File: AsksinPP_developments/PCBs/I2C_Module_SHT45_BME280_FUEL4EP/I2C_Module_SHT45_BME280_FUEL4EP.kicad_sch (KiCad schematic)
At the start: 14 parts, among them J1 Conn_01x04, J2 Conn_01x04, U1 BME280, U2 SHT45-AD1F-R2

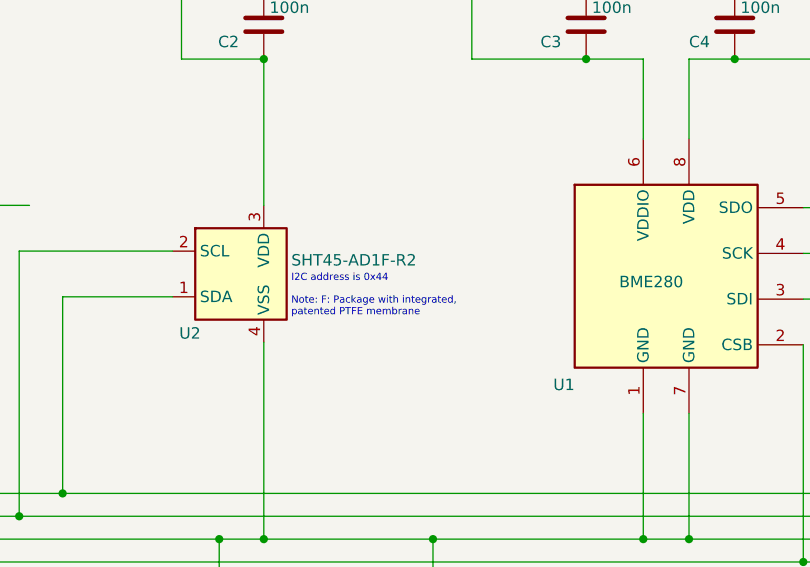
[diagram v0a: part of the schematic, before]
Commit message: PCBs: HB_TH_Sensor_SHT45_AllInOne_FUEL4EP and I2C_Module_SHT45_BME280_FUEL4EP: replacement of SHT45 to type without PTFE filter
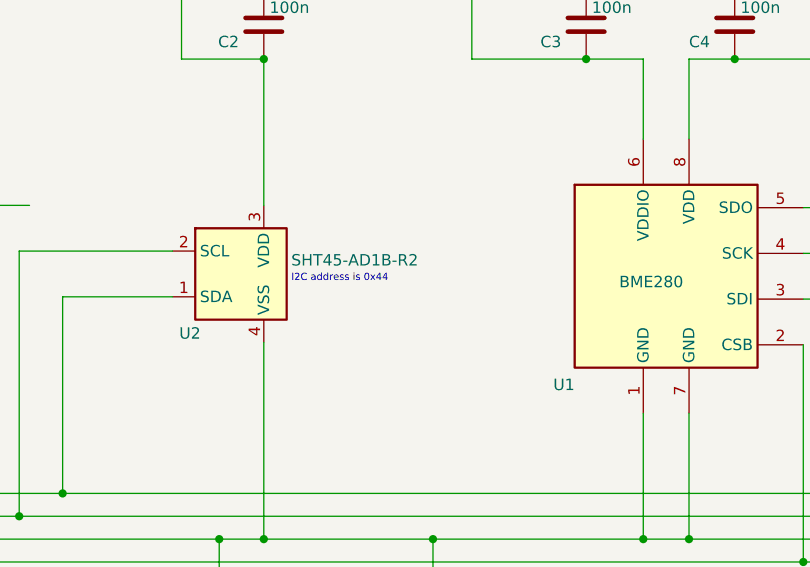
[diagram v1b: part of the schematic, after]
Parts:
- U2: value SHT45-AD1F-R2 -> SHT45-AD1B-R2; LCSC C5360602 -> C5221601
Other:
- note removed: "Note: F: Package with integrated, patented PTFE membrane"
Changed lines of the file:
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@@
   (title_block
     (title "I2C_Module_SHT45_BME280_FUEL4EP")
-    (date "2023-09-09")
-    (rev "1.0")
+    (date "2023-12-15")
+    (rev "1.1")
     (company "FUEL4EP")
     (comment 1 "fitting to  HB-UNI-SEN-BATT_ATMega1284P_E07-868MS10_FUEL4EP")
@@
     (stroke (width 0) (type default) (color 0 0 0 0))
   )
-  (text "Note: F: Package with integrated,\npatented PTFE membrane"
-    (at 105.664 87.122 0)
-    (effects (font (size 0.8 0.8)) (justify left bottom))
-  )
   (text "cut JP1 for I2C address 0x77\n" (at 163.83 74.295 0)
     (effects (font (size 0.8 0.8)) (justify left bottom))
@@
       (effects (font (size 1.27 1.27)) (justify left))
     )
-    (property "Value" "SHT45-AD1F-R2" (id 1) (at 105.664 80.772 0)
+    (property "Value" "SHT45-AD1B-R2" (id 1) (at 105.664 80.772 0)
       (effects (font (size 1.27 1.27)) (justify left))
     )
@@
       (effects (font (size 1.27 1.27)) (justify left) hide)
     )
-    (property "Datasheet" "https://sensirion.com/media/documents/33FD6951/624C4357/Datasheet_SHT4x.pdf" (id 3) (at 103.886 91.186 0)
+    (property "Datasheet" "https://sensirion.com/media/documents/33FD6951/6555C40E/Sensirion_Datasheet_SHT4x.pdf" (id 3) (at 103.886 91.186 0)
       (effects (font (size 1.27 1.27)) (justify left) hide)
     )
-    (property "LCSC" "C5360602" (id 4) (at 100.076 82.296 0)
+    (property "LCSC" "C5221601" (id 4) (at 100.076 82.296 0)
       (effects (font (size 1.524 1.524)) hide)
     )
@@
     )
     (path "/4286b13a-2c83-4a2b-871b-df5ad20905f3"
-      (reference "U2") (unit 1) (value "SHT45-AD1F-R2") (footprint "FUEL4EP:SHT4X")
-    )
-  )
+      (reference "U2") (unit 1) (value "SHT45-AD1B-R2") (footprint "FUEL4EP:SHT4X")
+    )
+  )

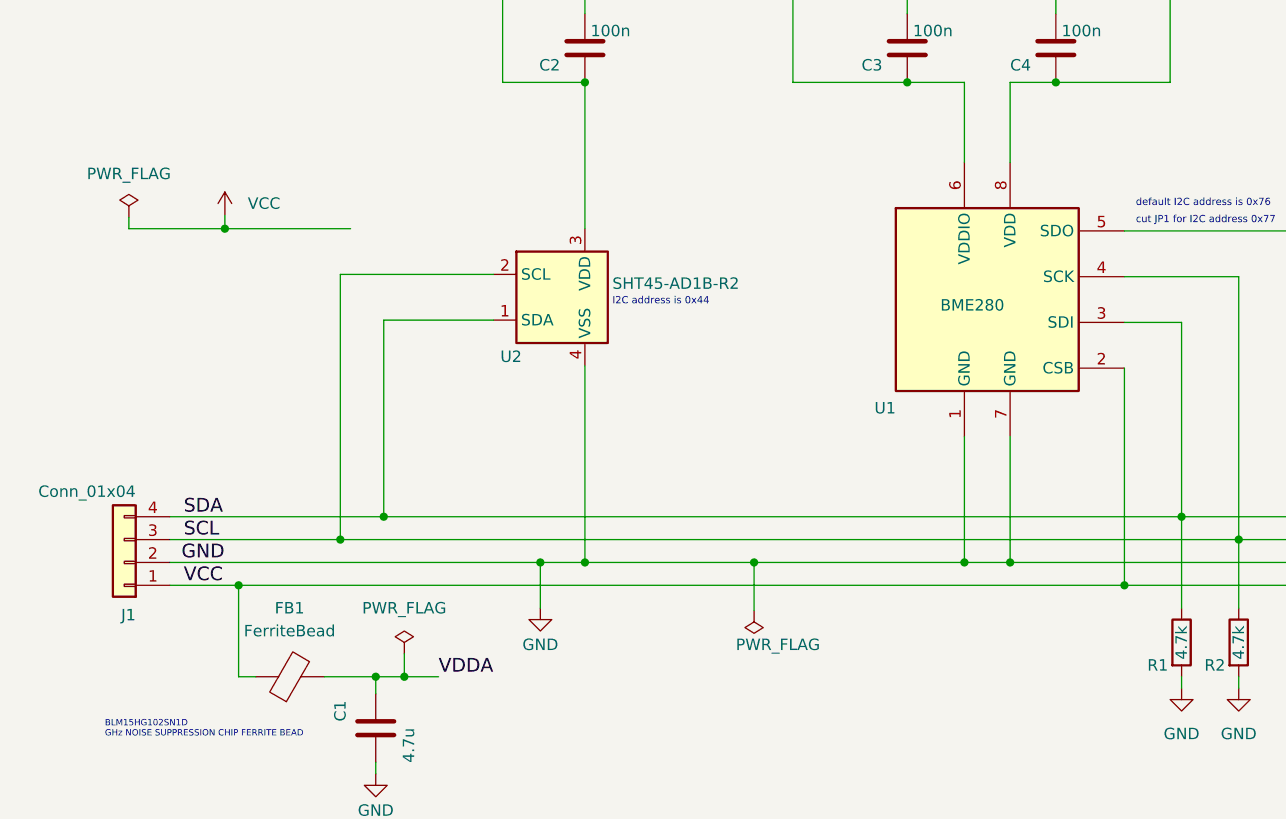
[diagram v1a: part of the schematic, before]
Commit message: PCBs: fix of some project specific KiCAD library paths for portability and missing PWR_FLGs for VCC in some schematics
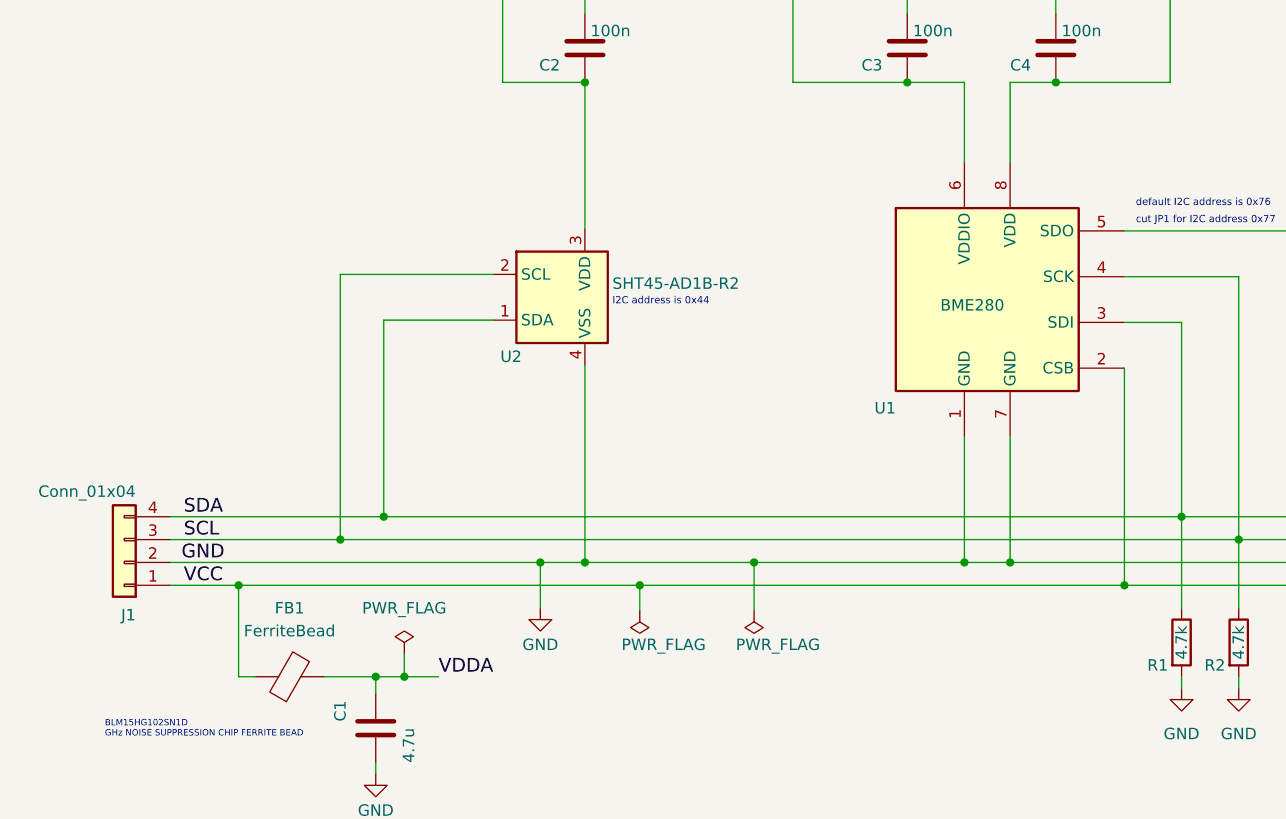
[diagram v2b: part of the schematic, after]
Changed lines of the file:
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@@
   (title_block
     (title "I2C_Module_SHT45_BME280_FUEL4EP")
-    (date "2023-12-15")
-    (rev "1.1")
+    (date "2024-01-14")
+    (rev "1.2")
     (company "FUEL4EP")
     (comment 1 "fitting to  HB-UNI-SEN-BATT_ATMega1284P_E07-868MS10_FUEL4EP")
@@
   (junction (at 149.86 111.76) (diameter 0) (color 0 0 0 0)
   )
-  (junction (at 62.611 74.676) (diameter 0) (color 0 0 0 0)
-  )
   (junction (at 154.94 58.42) (diameter 0) (color 0 0 0 0)
   )
@@
   (junction (at 82.55 124.46) (diameter 0) (color 0 0 0 0)
   )
+  (junction (at 108.712 114.3) (diameter 0) (color 0 0 0 0)
+  )
   (junction (at 102.616 111.76) (diameter 0) (color 0 0 0 0)
   )
@@
     (stroke (width 0) (type default) (color 0 0 0 0))
   )
-  (wire (pts (xy 51.943 74.676) (xy 51.943 73.406))
-    (stroke (width 0) (type default) (color 0 0 0 0))
-  )
   (wire (pts (xy 138.43 48.26) (xy 138.43 50.8))
     (stroke (width 0) (type default) (color 0 0 0 0))
@@
     (stroke (width 0) (type default) (color 0 0 0 0))
   )
-  (wire (pts (xy 62.611 74.676) (xy 51.943 74.676))
+  (wire (pts (xy 108.712 114.3) (xy 162.56 114.3))
     (stroke (width 0) (type default) (color 0 0 0 0))
   )
@@
     (stroke (width 0) (type default) (color 0 0 0 0))
   )
-  (wire (pts (xy 62.611 74.676) (xy 62.611 73.152))
-    (stroke (width 0) (type default) (color 0 0 0 0))
-  )
   (wire (pts (xy 125.73 58.42) (xy 138.43 58.42))
     (stroke (width 0) (type default) (color 0 0 0 0))
   )
-  (wire (pts (xy 64.135 114.3) (xy 162.56 114.3))
+  (wire (pts (xy 64.135 114.3) (xy 108.712 114.3))
     (stroke (width 0) (type default) (color 0 0 0 0))
   )
@@
     (stroke (width 0) (type default) (color 0 0 0 0))
   )
-  (wire (pts (xy 62.611 74.676) (xy 76.581 74.676))
-    (stroke (width 0) (type default) (color 0 0 0 0))
-  )
   (wire (pts (xy 56.515 111.76) (xy 97.663 111.76))
+    (stroke (width 0) (type default) (color 0 0 0 0))
+  )
+  (wire (pts (xy 108.712 114.3) (xy 108.712 117.094))
     (stroke (width 0) (type default) (color 0 0 0 0))
   )
@@
     (pin "8")
   )
-  (symbol (lib_id "power:VCC") (at 62.611 73.152 0) (unit 1)
-    (in_bom yes) (on_board yes) (fields_autoplaced)
-    (property "Reference" "#PWR01" (id 0) (at 62.611 76.962 0)
-      (effects (font (size 1.27 1.27)) hide)
-    )
-    (property "Value" "VCC" (id 1) (at 65.151 71.8819 0)
-      (effects (font (size 1.27 1.27)) (justify left))
-    )
-    (property "Footprint" "" (id 2) (at 62.611 73.152 0)
-      (effects (font (size 1.27 1.27)) hide)
-    )
-    (property "Datasheet" "" (id 3) (at 62.611 73.152 0)
-      (effects (font (size 1.27 1.27)) hide)
-    )
-    (pin "1")
-  )
   (symbol (lib_id "Device:C") (at 79.375 130.175 0) (unit 1)
     (in_bom yes) (on_board yes)
@@
     (pin "1")
   )
-  (symbol (lib_id "power:PWR_FLAG") (at 51.943 73.406 0) (unit 1)
-    (in_bom yes) (on_board yes) (fields_autoplaced)
-    (property "Reference" "#FLG01" (id 0) (at 51.943 71.501 0)
-      (effects (font (size 1.27 1.27)) hide)
-    )
-    (property "Value" "PWR_FLAG" (id 1) (at 51.943 68.58 0))
-    (property "Footprint" "" (id 2) (at 51.943 73.406 0)
-      (effects (font (size 1.27 1.27)) hide)
-    )
-    (property "Datasheet" "~" (id 3) (at 51.943 73.406 0)
-      (effects (font (size 1.27 1.27)) hide)
-    )
-    (pin "1")
-  )
   (symbol (lib_id "power:PWR_FLAG") (at 121.412 117.094 180) (unit 1)
     (in_bom yes) (on_board yes)
@@
     (pin "2")
   )
+  (symbol (lib_id "power:PWR_FLAG") (at 108.712 117.094 180) (unit 1)
+    (in_bom yes) (on_board yes)
+    (property "Reference" "#FLG0102" (id 0) (at 108.712 118.999 0)
+      (effects (font (size 1.27 1.27)) hide)
+    )
+    (property "Value" "PWR_FLAG" (id 1) (at 106.68 120.904 0)
+      (effects (font (size 1.27 1.27)) (justify right))
+    )
+    (property "Footprint" "" (id 2) (at 108.712 117.094 0)
+      (effects (font (size 1.27 1.27)) hide)
+    )
+    (property "Datasheet" "~" (id 3) (at 108.712 117.094 0)
+      (effects (font (size 1.27 1.27)) hide)
+    )
+    (pin "1")
+  )
   (sheet_instances
     (path "/" (page "1"))
   )
   (symbol_instances
-    (path "/accbd0c3-e588-4a03-8c25-5dc64064deb9"
-      (reference "#FLG01") (unit 1) (value "PWR_FLAG") (footprint "")
-    )
     (path "/b998681a-aa50-4b75-bf22-d9fbe42fce6f"
       (reference "#FLG02") (unit 1) (value "PWR_FLAG") (footprint "")
@@
       (reference "#FLG0101") (unit 1) (value "PWR_FLAG") (footprint "")
     )
-    (path "/71fc455e-be46-44e1-9ad6-6659dc653656"
-      (reference "#PWR01") (unit 1) (value "VCC") (footprint "")
+    (path "/f85138f1-4fc4-47b7-a48c-cc54b2d132a0"
+      (reference "#FLG0102") (unit 1) (value "PWR_FLAG") (footprint "")
     )
     (path "/2fb280af-9352-43f7-93d8-89326fb5dc6f"

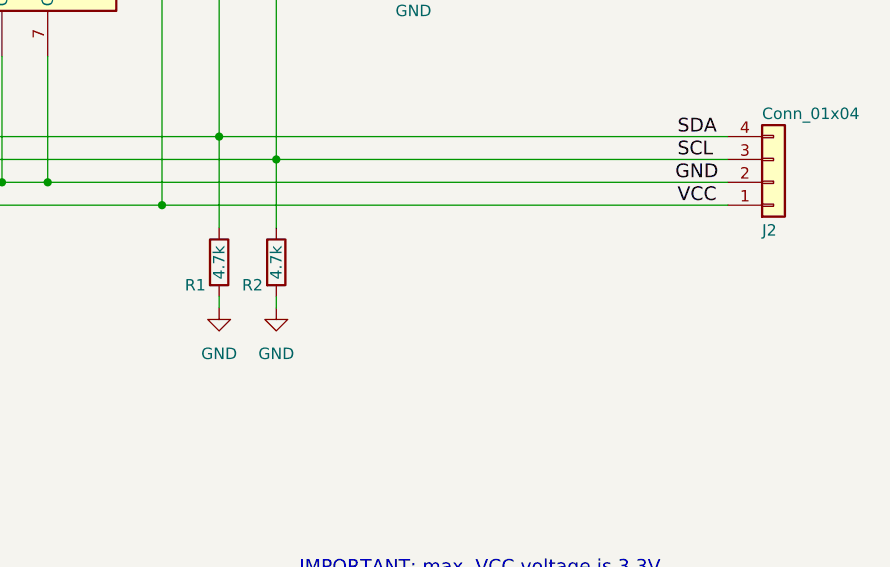
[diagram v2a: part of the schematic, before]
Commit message: PCBs: fix of I2C Pull-up resistors that were wrongly tied to GND
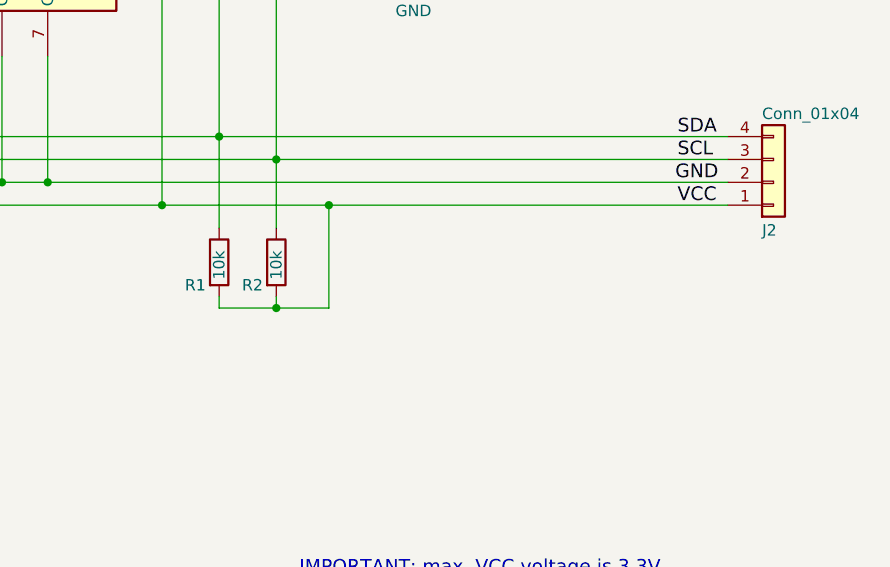
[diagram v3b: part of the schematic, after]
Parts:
- R1, R2: value 4.7k -> 10k; LCSC C25900 -> C25744
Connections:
- net GND: no longer R1.2, R2.2
- net VCC: now also R1.2, R2.2
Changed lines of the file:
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@@
   (title_block
     (title "I2C_Module_SHT45_BME280_FUEL4EP")
-    (date "2024-01-14")
-    (rev "1.2")
+    (date "2024-02-08")
+    (rev "1.3")
     (company "FUEL4EP")
     (comment 1 "fitting to  HB-UNI-SEN-BATT_ATMega1284P_E07-868MS10_FUEL4EP")
@@
   (junction (at 154.94 58.42) (diameter 0) (color 0 0 0 0)
   )
+  (junction (at 181.102 114.3) (diameter 0) (color 0 0 0 0)
+  )
   (junction (at 79.375 124.46) (diameter 0) (color 0 0 0 0)
   )
@@
   (junction (at 80.264 106.68) (diameter 0) (color 0 0 0 0)
   )
+  (junction (at 175.26 125.73) (diameter 0) (color 0 0 0 0)
+  )
   (junction (at 168.91 106.68) (diameter 0) (color 0 0 0 0)
   )
@@
     (stroke (width 0) (type default) (color 0 0 0 0))
   )
+  (wire (pts (xy 175.26 125.73) (xy 181.102 125.73))
+    (stroke (width 0) (type default) (color 0 0 0 0))
+  )
   (wire (pts (xy 162.56 85.09) (xy 168.91 85.09))
     (stroke (width 0) (type default) (color 0 0 0 0))
@@
     (stroke (width 0) (type default) (color 0 0 0 0))
   )
+  (wire (pts (xy 181.102 125.73) (xy 181.102 114.3))
+    (stroke (width 0) (type default) (color 0 0 0 0))
+  )
   (wire (pts (xy 149.86 58.42) (xy 154.94 58.42))
     (stroke (width 0) (type default) (color 0 0 0 0))
@@
     (stroke (width 0) (type default) (color 0 0 0 0))
   )
+  (wire (pts (xy 181.102 114.3) (xy 225.425 114.3))
+    (stroke (width 0) (type default) (color 0 0 0 0))
+  )
   (wire (pts (xy 154.94 58.42) (xy 167.64 58.42))
     (stroke (width 0) (type default) (color 0 0 0 0))
@@
     (stroke (width 0) (type default) (color 0 0 0 0))
   )
+  (wire (pts (xy 168.91 125.73) (xy 175.26 125.73))
+    (stroke (width 0) (type default) (color 0 0 0 0))
+  )
   (wire (pts (xy 64.135 124.46) (xy 66.04 124.46))
     (stroke (width 0) (type default) (color 0 0 0 0))
@@
     (stroke (width 0) (type default) (color 0 0 0 0))
   )
-  (wire (pts (xy 162.56 114.3) (xy 225.425 114.3))
+  (wire (pts (xy 162.56 114.3) (xy 181.102 114.3))
     (stroke (width 0) (type default) (color 0 0 0 0))
   )
@@
       (effects (font (size 1.27 1.27)) (justify left))
     )
-    (property "Value" "4.7k" (id 1) (at 168.91 122.555 90)
+    (property "Value" "10k" (id 1) (at 168.91 122.555 90)
       (effects (font (size 1.27 1.27)) (justify left))
     )
@@
       (effects (font (size 1.27 1.27)) hide)
     )
-    (property "LCSC" "C25900" (id 4) (at 168.91 120.65 0)
+    (property "LCSC" "C25744" (id 4) (at 168.91 120.65 0)
       (effects (font (size 1.524 1.524)) hide)
     )
@@
     )
     (property "Datasheet" "" (id 3) (at 93.472 48.768 0)
-      (effects (font (size 1.27 1.27)) hide)
-    )
-    (pin "1")
-  )
-  (symbol (lib_id "power:GND") (at 168.91 125.73 0) (unit 1)
-    (in_bom yes) (on_board yes) (fields_autoplaced)
-    (property "Reference" "#PWR07" (id 0) (at 168.91 132.08 0)
-      (effects (font (size 1.27 1.27)) hide)
-    )
-    (property "Value" "GND" (id 1) (at 168.91 130.81 0))
-    (property "Footprint" "" (id 2) (at 168.91 125.73 0)
-      (effects (font (size 1.27 1.27)) hide)
-    )
-    (property "Datasheet" "" (id 3) (at 168.91 125.73 0)
       (effects (font (size 1.27 1.27)) hide)
     )
@@
     (pin "1")
   )
-  (symbol (lib_id "power:GND") (at 175.26 125.73 0) (unit 1)
-    (in_bom yes) (on_board yes) (fields_autoplaced)
-    (property "Reference" "#PWR08" (id 0) (at 175.26 132.08 0)
-      (effects (font (size 1.27 1.27)) hide)
-    )
-    (property "Value" "GND" (id 1) (at 175.26 130.81 0))
-    (property "Footprint" "" (id 2) (at 175.26 125.73 0)
-      (effects (font (size 1.27 1.27)) hide)
-    )
-    (property "Datasheet" "" (id 3) (at 175.26 125.73 0)
-      (effects (font (size 1.27 1.27)) hide)
-    )
-    (pin "1")
-  )
   (symbol (lib_id "power:VDDA") (at 167.64 48.26 0) (unit 1)
     (in_bom yes) (on_board yes) (fields_autoplaced)
@@
       (effects (font (size 1.27 1.27)) (justify left))
     )
-    (property "Value" "4.7k" (id 1) (at 175.26 122.555 90)
+    (property "Value" "10k" (id 1) (at 175.26 122.555 90)
       (effects (font (size 1.27 1.27)) (justify left))
     )
@@
       (effects (font (size 1.27 1.27)) hide)
     )
-    (property "LCSC" "C25900" (id 4) (at 175.26 120.65 0)
+    (property "LCSC" "C25744" (id 4) (at 175.26 120.65 0)
       (effects (font (size 1.524 1.524)) hide)
     )
@@
       (reference "#PWR06") (unit 1) (value "VDDA") (footprint "")
     )
-    (path "/18542ab6-239f-4332-a70c-3c8551b285bb"
-      (reference "#PWR07") (unit 1) (value "GND") (footprint "")
-    )
-    (path "/d43541cc-8fb7-4c57-a7c8-5b5588c55acf"
-      (reference "#PWR08") (unit 1) (value "GND") (footprint "")
-    )
     (path "/b9ee5250-0210-4fd4-abf8-6419214a066d"
       (reference "#PWR09") (unit 1) (value "GND") (footprint "")
@@
     )
     (path "/010452d5-e5f2-447e-a153-71da0dbec114"
-      (reference "R1") (unit 1) (value "4.7k") (footprint "Resistor_SMD:R_0402_1005Metric")
+      (reference "R1") (unit 1) (value "10k") (footprint "Resistor_SMD:R_0402_1005Metric")
     )
     (path "/f75dc7be-70bf-4119-8c06-195e1a960dd2"
-      (reference "R2") (unit 1) (value "4.7k") (footprint "Resistor_SMD:R_0402_1005Metric")
+      (reference "R2") (unit 1) (value "10k") (footprint "Resistor_SMD:R_0402_1005Metric")
     )
     (path "/55b96afd-ec19-4400-9134-cc56302d872a"
